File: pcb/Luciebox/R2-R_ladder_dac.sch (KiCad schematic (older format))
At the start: 12 parts, among them T2 terminal_8x1, T3 terminal_8x1, T4 terminal_8x1

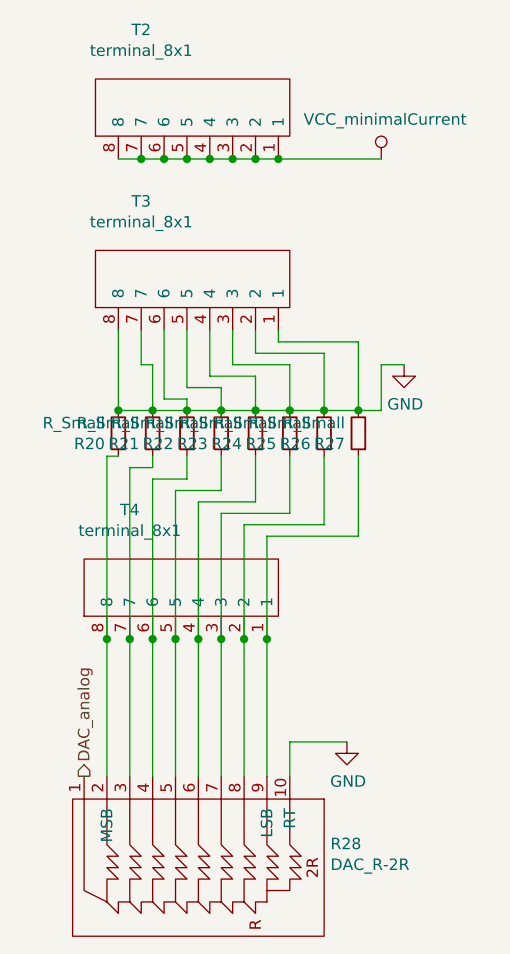
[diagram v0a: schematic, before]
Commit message: modify pcb v2.0.  nearly finished. Choose box.
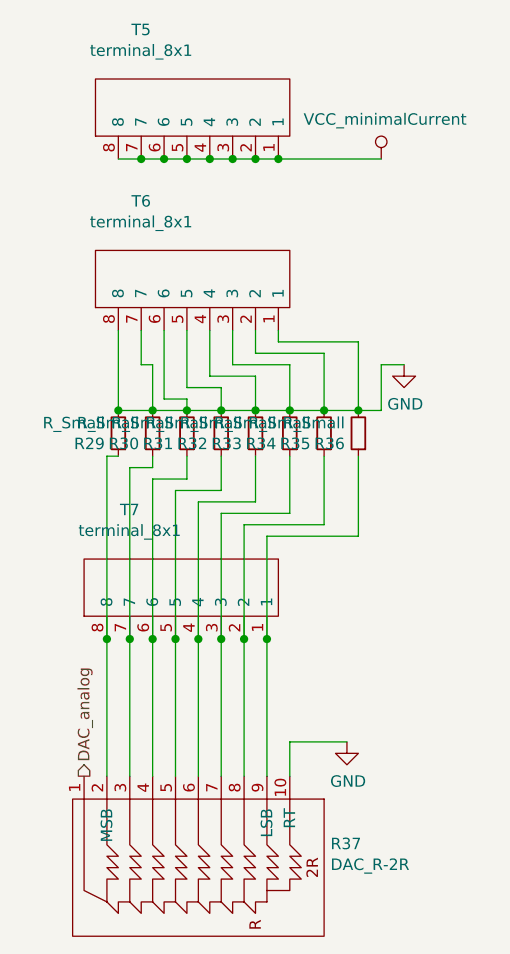
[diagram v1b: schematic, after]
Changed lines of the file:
@@
 AR Path="/5D761BCA/5D7526CF" Ref="R36"  Part="1"
 AR Path="/5D9307E8/5D7526CF" Ref="R45"  Part="1"
-F 0 "R27" H 3709 2246 50  0000 L CNN
+F 0 "R36" H 3709 2246 50  0000 L CNN
 F 1 "R_Small" H 3709 2155 50  0000 L CNN
 F 2 "Luciebox:1206_0805" H 3650 2200 50  0001 C CNN
@@
 AR Path="/5D761BCA/5E6454DF" Ref="R35"  Part="1"
 AR Path="/5D9307E8/5E6454DF" Ref="R44"  Part="1"
-F 0 "R26" H 3559 2246 50  0000 L CNN
+F 0 "R35" H 3559 2246 50  0000 L CNN
 F 1 "R_Small" H 3559 2155 50  0000 L CNN
 F 2 "Luciebox:1206_0805" H 3500 2200 50  0001 C CNN
@@
 AR Path="/5D761BCA/5E6454E0" Ref="R34"  Part="1"
 AR Path="/5D9307E8/5E6454E0" Ref="R43"  Part="1"
-F 0 "R25" H 3409 2246 50  0000 L CNN
+F 0 "R34" H 3409 2246 50  0000 L CNN
 F 1 "R_Small" H 3409 2155 50  0000 L CNN
 F 2 "Luciebox:1206_0805" H 3350 2200 50  0001 C CNN
@@
 AR Path="/5D761BCA/5E6454E1" Ref="R33"  Part="1"
 AR Path="/5D9307E8/5E6454E1" Ref="R42"  Part="1"
-F 0 "R24" H 3259 2246 50  0000 L CNN
+F 0 "R33" H 3259 2246 50  0000 L CNN
 F 1 "R_Small" H 3259 2155 50  0000 L CNN
 F 2 "Luciebox:1206_0805" H 3200 2200 50  0001 C CNN
@@
 AR Path="/5D761BCA/5D7526ED" Ref="R32"  Part="1"
 AR Path="/5D9307E8/5D7526ED" Ref="R41"  Part="1"
-F 0 "R23" H 3109 2246 50  0000 L CNN
+F 0 "R32" H 3109 2246 50  0000 L CNN
 F 1 "R_Small" H 3109 2155 50  0000 L CNN
 F 2 "Luciebox:1206_0805" H 3050 2200 50  0001 C CNN
@@
 AR Path="/5D761BCA/5D7526F3" Ref="R31"  Part="1"
 AR Path="/5D9307E8/5D7526F3" Ref="R40"  Part="1"
-F 0 "R22" H 2959 2246 50  0000 L CNN
+F 0 "R31" H 2959 2246 50  0000 L CNN
 F 1 "R_Small" H 2959 2155 50  0000 L CNN
 F 2 "Luciebox:1206_0805" H 2900 2200 50  0001 C CNN
@@
 AR Path="/5D761BCA/5D7526F9" Ref="R30"  Part="1"
 AR Path="/5D9307E8/5D7526F9" Ref="R39"  Part="1"
-F 0 "R21" H 2809 2246 50  0000 L CNN
+F 0 "R30" H 2809 2246 50  0000 L CNN
 F 1 "R_Small" H 2809 2155 50  0000 L CNN
 F 2 "Luciebox:1206_0805" H 2750 2200 50  0001 C CNN
@@
 AR Path="/5D761BCA/5D7527B8" Ref="R29"  Part="1"
 AR Path="/5D9307E8/5D7527B8" Ref="R38"  Part="1"
-F 0 "R20" H 2659 2246 50  0000 L CNN
+F 0 "R29" H 2659 2246 50  0000 L CNN
 F 1 "R_Small" H 2659 2155 50  0000 L CNN
 F 2 "Luciebox:1206_0805" H 2600 2200 50  0001 C CNN
@@
 AR Path="/5D761BCA/5E6454E2" Ref="R37"  Part="1"
 AR Path="/5D9307E8/5E6454E2" Ref="R46"  Part="1"
-F 0 "R28" V 2746 4778 50  0000 L CNN
+F 0 "R37" V 2746 4778 50  0000 L CNN
 F 1 "DAC_R-2R" V 2837 4778 50  0000 L CNN
 F 2 "Luciebox:SIP-10" H 2450 3700 50  0001 C CNN
@@
 AR Path="/5D761BCA/5D7526D5" Ref="T7"  Part="1"
 AR Path="/5D9307E8/5D7526D5" Ref="T10"  Part="1"
-F 0 "T4" V 3765 3650 50  0000 C CNN
+F 0 "T7" V 3765 3650 50  0000 C CNN
 F 1 "terminal_8x1" V 3674 3650 50  0000 C CNN
 F 2 "Luciebox:Terminal_8x1_100mil" H 3250 3050 50  0001 C CNN
@@
 AR Path="/5D761BCA/5DAEA72B" Ref="T6"  Part="1"
 AR Path="/5D9307E8/5DAEA72B" Ref="T9"  Part="1"
-F 0 "T3" V 3815 2300 50  0000 C CNN
+F 0 "T6" V 3815 2300 50  0000 C CNN
 F 1 "terminal_8x1" V 3724 2300 50  0000 C CNN
 F 2 "Luciebox:Terminal_8x1_100mil" H 3300 1700 50  0001 C CNN
@@
 AR Path="/5D761BCA/5DB0039D" Ref="T5"  Part="1"
 AR Path="/5D9307E8/5DB0039D" Ref="T8"  Part="1"
-F 0 "T2" V 3815 1550 50  0000 C CNN
+F 0 "T5" V 3815 1550 50  0000 C CNN
 F 1 "terminal_8x1" V 3724 1550 50  0000 C CNN
 F 2 "Luciebox:Terminal_8x1_100mil" H 3300 950 50  0001 C CNN
